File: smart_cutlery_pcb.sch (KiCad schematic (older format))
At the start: 0 parts

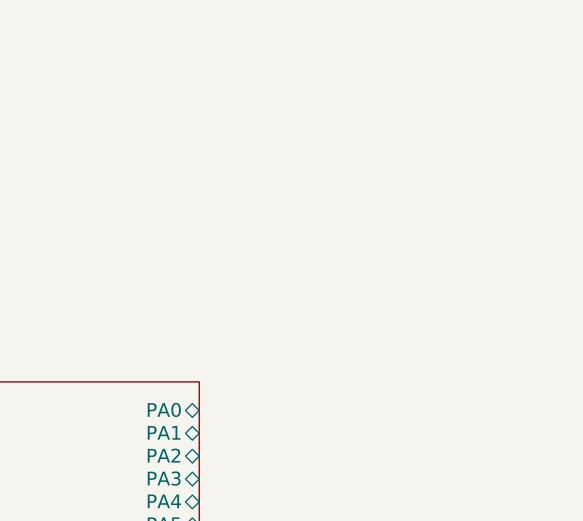
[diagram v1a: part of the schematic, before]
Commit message: Capture boost converter, soft latching power
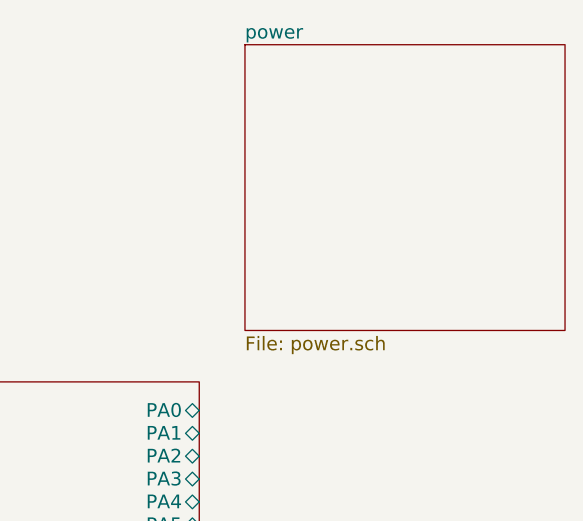
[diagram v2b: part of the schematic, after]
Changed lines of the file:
@@
 LIBS:stm32
 LIBS:bluetooth_hc-05
+LIBS:mechanical
+LIBS:switches
+LIBS:NCP1402SN33T1G
+LIBS:diode
 LIBS:smart_cutlery_pcb-cache
 EELAYER 25 0
@@
 $Descr A4 11693 8268
 encoding utf-8
-Sheet 1 3
+Sheet 1 4
 Title ""
 Date ""
@@
 F3 "BLUETOOTH_RX" I R 3750 2450 60
 $EndSheet
+$Sheet
+S 7300 1400 1400 1250
+U 59A1225E
+F0 "power" 60
+F1 "power.sch" 60
+$EndSheet
 $EndSCHEMATC

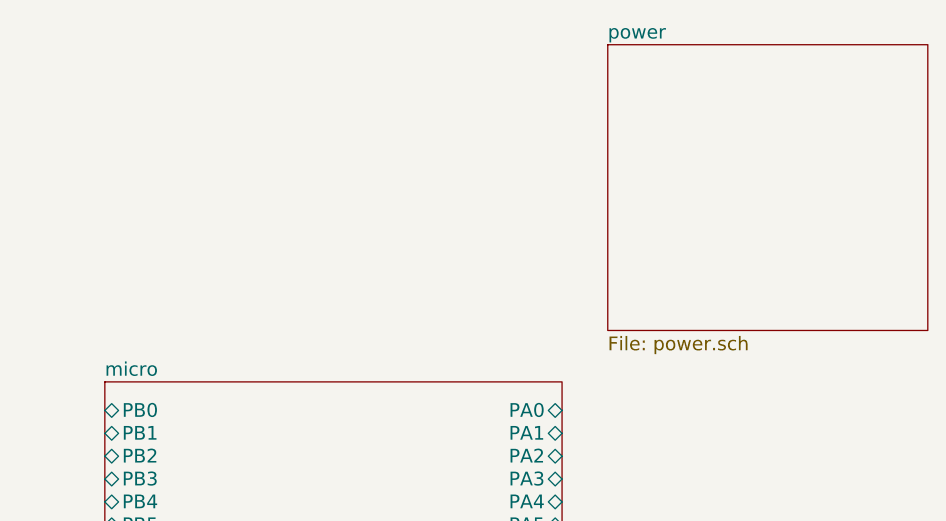
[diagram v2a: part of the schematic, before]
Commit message: Add accelerometer/gyro
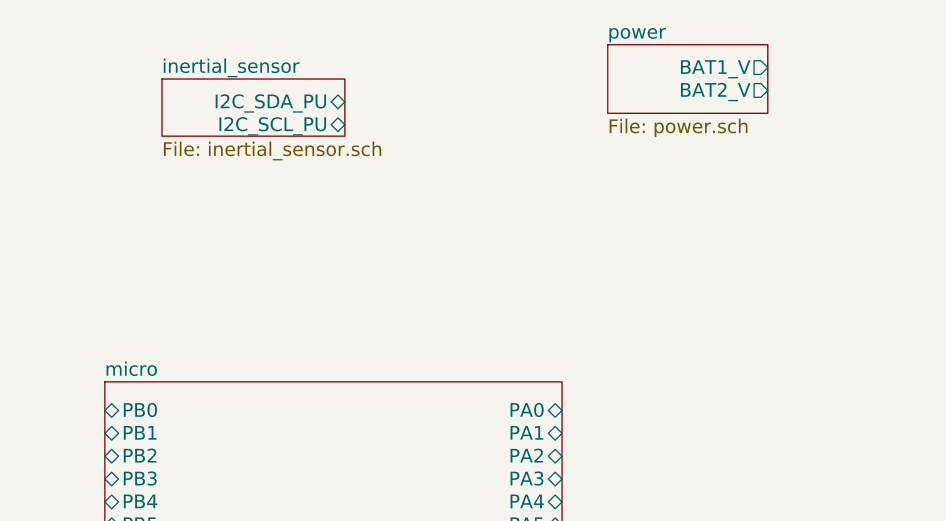
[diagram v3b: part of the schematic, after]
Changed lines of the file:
@@
 LIBS:NCP1402SN33T1G
 LIBS:diode
+LIBS:battery_management
+LIBS:sensors
 LIBS:smart_cutlery_pcb-cache
 EELAYER 25 0
@@
 $Descr A4 11693 8268
 encoding utf-8
-Sheet 1 4
+Sheet 1 5
 Title ""
 Date ""
@@
 $EndSheet
 $Sheet
-S 7300 1400 1400 1250
+S 7300 1400 700  300
 U 59A1225E
 F0 "power" 60
 F1 "power.sch" 60
+F2 "BAT1_V" O R 8000 1500 60
+F3 "BAT2_V" O R 8000 1600 60
+$EndSheet
+$Sheet
+S 5350 1550 800  250
+U 59A2044A
+F0 "inertial_sensor" 60
+F1 "inertial_sensor.sch" 60
+F2 "I2C_SDA_PU" B R 6150 1650 60
+F3 "I2C_SCL_PU" B R 6150 1750 60
 $EndSheet
 $EndSCHEMATC
